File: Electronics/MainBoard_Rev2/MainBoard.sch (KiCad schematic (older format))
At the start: 18 parts, among them J1 Conn_01x04_Female, J2 DB9_Female, U1 ESP32-WROOM-32

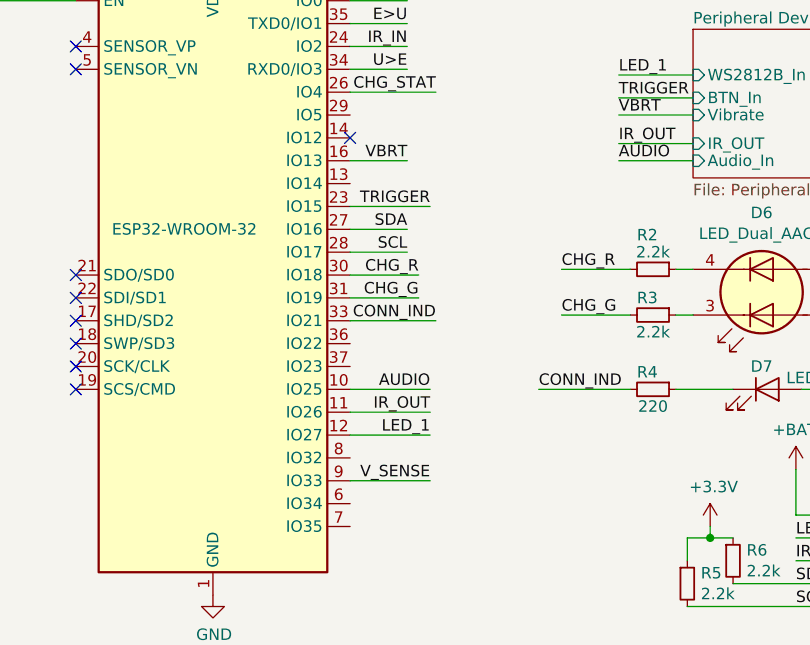
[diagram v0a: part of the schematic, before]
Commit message: Began preparing a branch for HackADay users
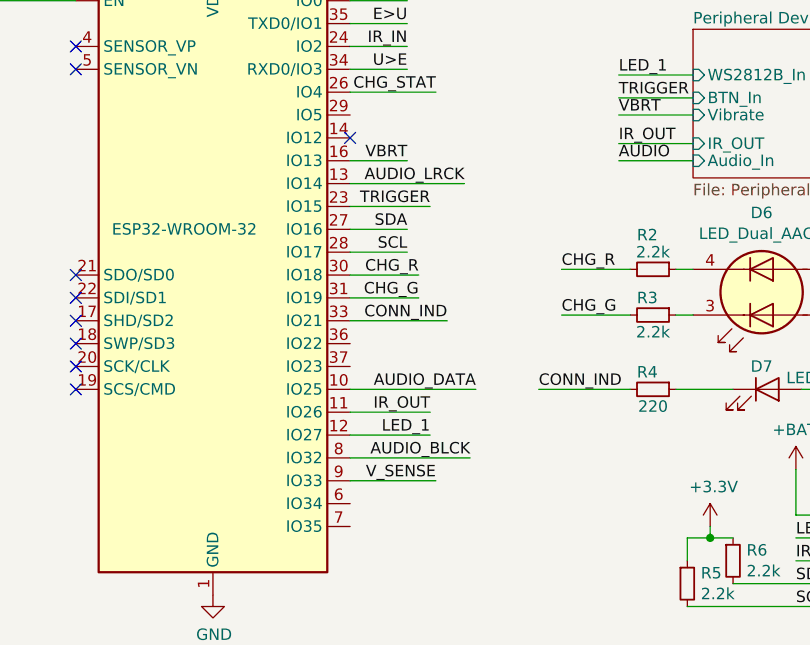
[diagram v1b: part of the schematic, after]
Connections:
- net AUDIO: no longer U1.10 (IO25)
- net AUDIO_LRCK: now reaches U1.13 (IO14)
- net AUDIO_BLCK: now reaches U1.8 (IO32)
- new net AUDIO_DATA: U1.10 (IO25)
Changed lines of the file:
@@
 $EndComp
 Wire Wire Line
-	6550 4000 6900 4000
-Text Label 6900 4000 2    50   ~ 0
-AUDIO
+	6550 4000 7100 4000
+Text Label 7100 4000 2    50   ~ 0
+AUDIO_DATA
 Text Label 7725 3000 0    50   ~ 0
 AUDIO
@@
 Text Label 8500 4650 0    50   ~ 0
 LED_2
-Text Label 6900 4400 2    50   ~ 0
+Text Label 6925 4400 2    50   ~ 0
 V_SENSE
 Wire Wire Line
@@
 V_SENSE
 Wire Wire Line
-	6900 4400 6550 4400
+	6925 4400 6550 4400
 Wire Wire Line
 	6550 3000 6800 3000
@@
 $EndComp
 Wire Wire Line
-	6550 3700 6925 3700
-Text Label 6925 3700 2    50   ~ 0
+	6550 3700 6975 3700
+Text Label 6975 3700 2    50   ~ 0
 CONN_IND
 Wire Wire Line
@@
 Wire Wire Line
 	2600 3575 2600 4325
+Wire Wire Line
+	6550 4300 7075 4300
+Text Label 7075 4300 2    50   ~ 0
+AUDIO_BLCK
+Wire Wire Line
+	6550 3100 7050 3100
+Text Label 7050 3100 2    50   ~ 0
+AUDIO_LRCK
 $EndSCHEMATC
